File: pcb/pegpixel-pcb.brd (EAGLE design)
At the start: 23.1 x 17.2 mm, 14 parts

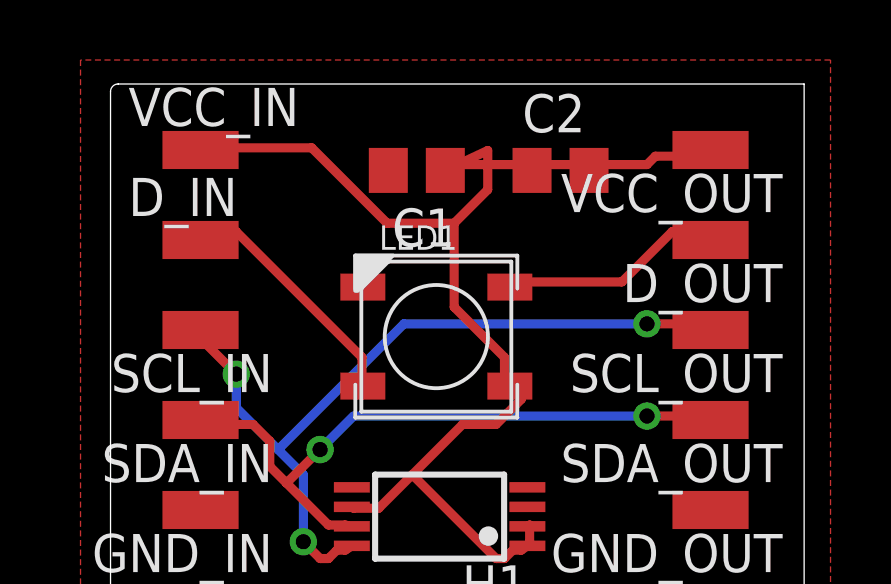
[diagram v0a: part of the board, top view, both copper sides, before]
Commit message: Add second capacitor to schema #2
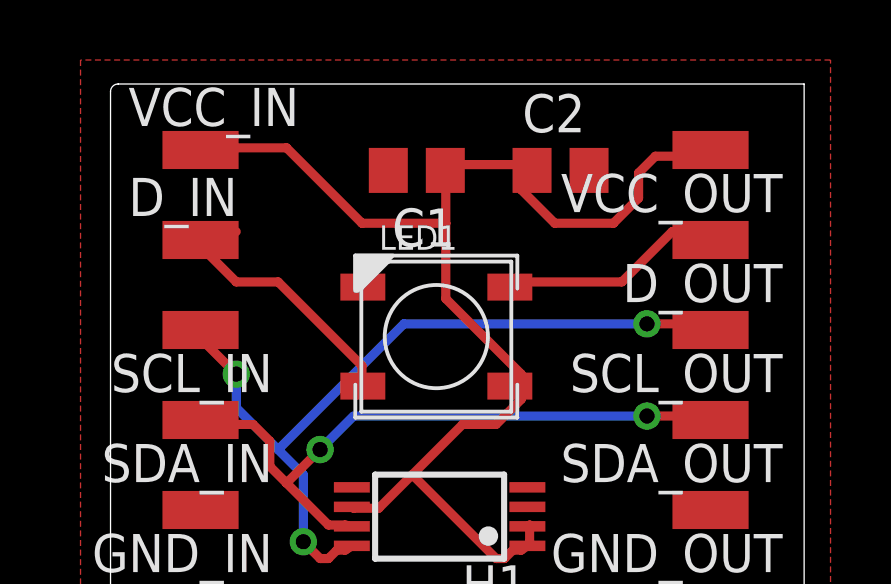
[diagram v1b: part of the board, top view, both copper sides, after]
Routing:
- net N$2: track 43.3 -> 44.7 mm
- net N$6: track 8.29 -> 9.62 mm
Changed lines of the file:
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@@
 <contactref element="VCC_IN" pad="1"/>
 <contactref element="VCC_OUT" pad="1"/>
+<contactref element="C2" pad="1"/>
+<wire x1="13.97" y1="21.5138" x2="13.6906" y2="21.5138" width="0.3048" layer="1"/>
+<wire x1="13.6906" y1="21.5138" x2="11.176" y2="21.5138" width="0.3048" layer="1"/>
+<wire x1="11.176" y1="21.5138" x2="11.16" y2="21.32" width="0.3048" layer="1"/>
+<wire x1="13.97" y1="21.5138" x2="14.05" y2="21.32" width="0.3048" layer="1"/>
 <wire x1="13.97" y1="9.4996" x2="13.97" y2="8.9408" width="0.3048" layer="1"/>
 <wire x1="13.97" y1="8.9408" x2="13.895" y2="8.805" width="0.3048" layer="1"/>
@@
 <wire x1="10.0584" y1="11.176" x2="12.8524" y2="8.382" width="0.3048" layer="1"/>
 <wire x1="13.6906" y1="8.6614" x2="13.895" y2="8.805" width="0.3048" layer="1"/>
-<wire x1="17.8816" y1="21.5138" x2="12.573" y2="21.5138" width="0.3048" layer="1"/>
-<wire x1="12.573" y1="21.5138" x2="11.2936" y2="21.5138" width="0.3048" layer="1"/>
-<wire x1="18.161" y1="21.7932" x2="17.8816" y2="21.5138" width="0.3048" layer="1"/>
-<wire x1="19.8374" y1="21.7932" x2="18.161" y2="21.7932" width="0.3048" layer="1"/>
-<wire x1="11.2936" y1="21.5138" x2="11.16" y2="21.32" width="0.3048" layer="1"/>
+<wire x1="11.176" y1="17.0434" x2="11.176" y2="19.558" width="0.3048" layer="1"/>
+<wire x1="11.176" y1="19.558" x2="11.176" y2="21.2344" width="0.3048" layer="1"/>
+<wire x1="13.6906" y1="14.5288" x2="11.176" y2="17.0434" width="0.3048" layer="1"/>
+<wire x1="13.6906" y1="13.97" x2="13.6906" y2="14.5288" width="0.3048" layer="1"/>
+<wire x1="11.176" y1="21.2344" x2="11.16" y2="21.32" width="0.3048" layer="1"/>
+<wire x1="13.6906" y1="13.97" x2="13.31" y2="14.13" width="0.3048" layer="1"/>
+<wire x1="5.8674" y1="22.0726" x2="3.0734" y2="22.0726" width="0.3048" layer="1"/>
+<wire x1="8.382" y1="19.558" x2="5.8674" y2="22.0726" width="0.3048" layer="1"/>
+<wire x1="11.176" y1="19.558" x2="8.382" y2="19.558" width="0.3048" layer="1"/>
+<wire x1="3.0734" y1="22.0726" x2="3" y2="22" width="0.3048" layer="1"/>
+<wire x1="18.161" y1="21.7932" x2="19.8374" y2="21.7932" width="0.3048" layer="1"/>
+<wire x1="17.6022" y1="21.2344" x2="18.161" y2="21.7932" width="0.3048" layer="1"/>
+<wire x1="17.6022" y1="20.3962" x2="17.6022" y2="21.2344" width="0.3048" layer="1"/>
+<wire x1="16.764" y1="19.558" x2="17.6022" y2="20.3962" width="0.3048" layer="1"/>
+<wire x1="14.8082" y1="19.558" x2="16.764" y2="19.558" width="0.3048" layer="1"/>
+<wire x1="13.6906" y1="20.6756" x2="14.8082" y2="19.558" width="0.3048" layer="1"/>
+<wire x1="13.6906" y1="21.5138" x2="13.6906" y2="20.6756" width="0.3048" layer="1"/>
 <wire x1="19.8374" y1="21.7932" x2="20" y2="22" width="0.3048" layer="1"/>
-<wire x1="6.7056" y1="22.0726" x2="3.0734" y2="22.0726" width="0.3048" layer="1"/>
-<wire x1="9.2202" y1="19.558" x2="6.7056" y2="22.0726" width="0.3048" layer="1"/>
-<wire x1="11.4554" y1="19.558" x2="9.2202" y2="19.558" width="0.3048" layer="1"/>
-<wire x1="12.573" y1="20.6756" x2="11.4554" y2="19.558" width="0.3048" layer="1"/>
-<wire x1="12.573" y1="21.98305" x2="12.573" y2="21.5138" width="0.3048" layer="1"/>
-<wire x1="12.573" y1="21.5138" x2="12.573" y2="20.6756" width="0.3048" layer="1"/>
-<wire x1="3.0734" y1="22.0726" x2="3" y2="22" width="0.3048" layer="1"/>
-<wire x1="12.573" y1="21.98305" x2="11.16" y2="21.32" width="0.3048" layer="1"/>
-<wire x1="13.1318" y1="15.0876" x2="13.1318" y2="14.2494" width="0.3048" layer="1"/>
-<wire x1="11.4554" y1="16.764" x2="13.1318" y2="15.0876" width="0.3048" layer="1"/>
-<wire x1="11.4554" y1="19.558" x2="11.4554" y2="16.764" width="0.3048" layer="1"/>
-<wire x1="13.1318" y1="14.2494" x2="13.31" y2="14.13" width="0.3048" layer="1"/>
-<contactref element="C2" pad="1"/>
-<wire x1="14.05" y1="21.32" x2="8.045" y2="10.105" width="0" layer="19" extent="1-1"/>
+<wire x1="13.6906" y1="21.5138" x2="14.05" y2="21.32" width="0.3048" layer="1"/>
 </signal>
 <signal name="N$4">
@@
 <contactref element="LED1" pad="4-DIN"/>
 <contactref element="D_IN" pad="1"/>
-<wire x1="8.382" y1="15.0876" x2="8.382" y2="14.2494" width="0.3048" layer="1"/>
-<wire x1="4.191" y1="19.2786" x2="8.382" y2="15.0876" width="0.3048" layer="1"/>
 <wire x1="3.0734" y1="19.2786" x2="4.191" y2="19.2786" width="0.3048" layer="1"/>
+<wire x1="3.0734" y1="19.2786" x2="3" y2="19" width="0.3048" layer="1"/>
+<wire x1="8.382" y1="14.8082" x2="8.382" y2="14.2494" width="0.3048" layer="1"/>
+<wire x1="5.588" y1="17.6022" x2="8.382" y2="14.8082" width="0.3048" layer="1"/>
+<wire x1="4.191" y1="17.6022" x2="5.588" y2="17.6022" width="0.3048" layer="1"/>
+<wire x1="2.794" y1="18.9992" x2="4.191" y2="17.6022" width="0.3048" layer="1"/>
 <wire x1="8.382" y1="14.2494" x2="8.41" y2="14.13" width="0.3048" layer="1"/>
-<wire x1="3.0734" y1="19.2786" x2="3" y2="19" width="0.3048" layer="1"/>
+<wire x1="2.794" y1="18.9992" x2="3" y2="19" width="0.3048" layer="1"/>
 </signal>
 <signal name="N$7">
@@
 </polygon>
 <contactref element="C2" pad="2"/>
-<wire x1="8.41" y1="17.43" x2="9.26" y2="21.32" width="0" layer="19" extent="1-1"/>
-<wire x1="13.895" y1="10.105" x2="8.41" y2="17.43" width="0" layer="19" extent="1-1"/>
-<wire x1="20" y1="10" x2="13.895" y2="10.105" width="0" layer="19" extent="1-1"/>
-<wire x1="3" y1="10" x2="8.41" y2="17.43" width="0" layer="19" extent="1-1"/>
-<wire x1="15.95" y1="21.32" x2="3" y2="10" width="0" layer="19" extent="1-1"/>
 </signal>
 </signals>

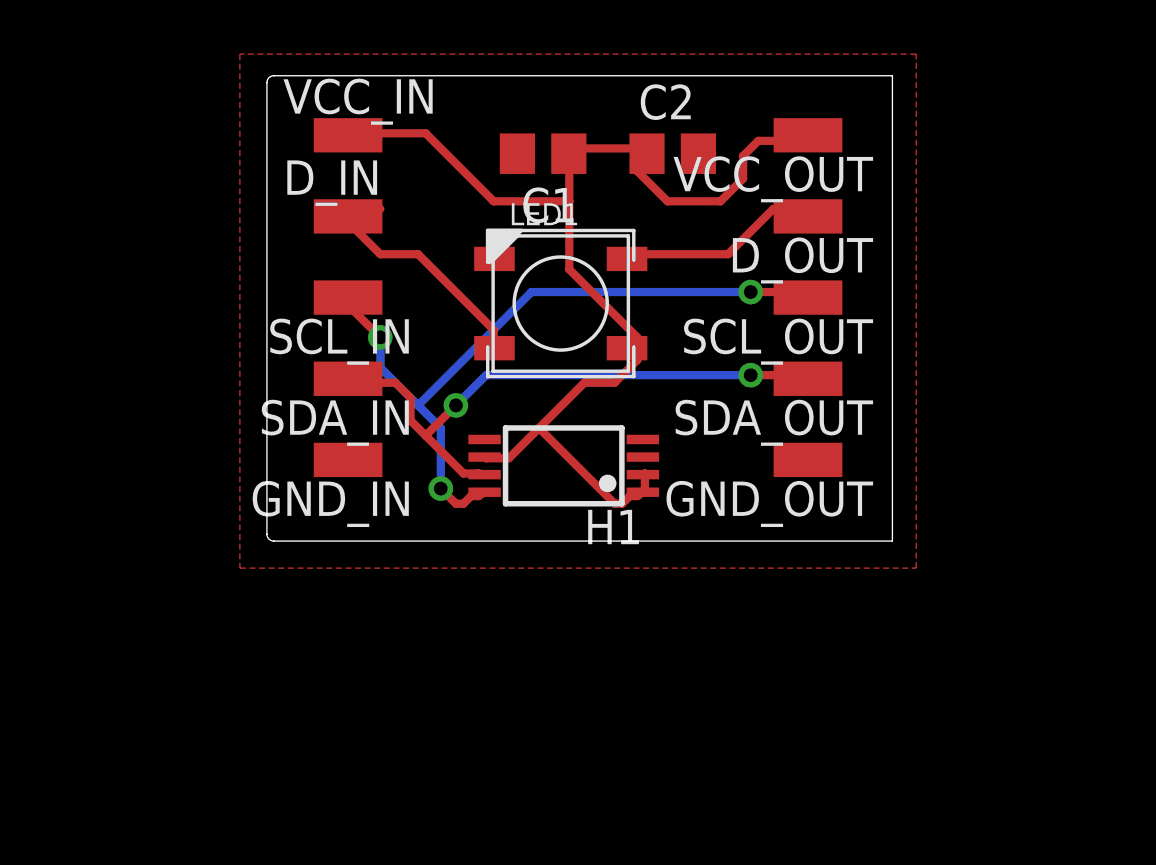
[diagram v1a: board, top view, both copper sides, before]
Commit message: pcb-design: delete design with solder-points
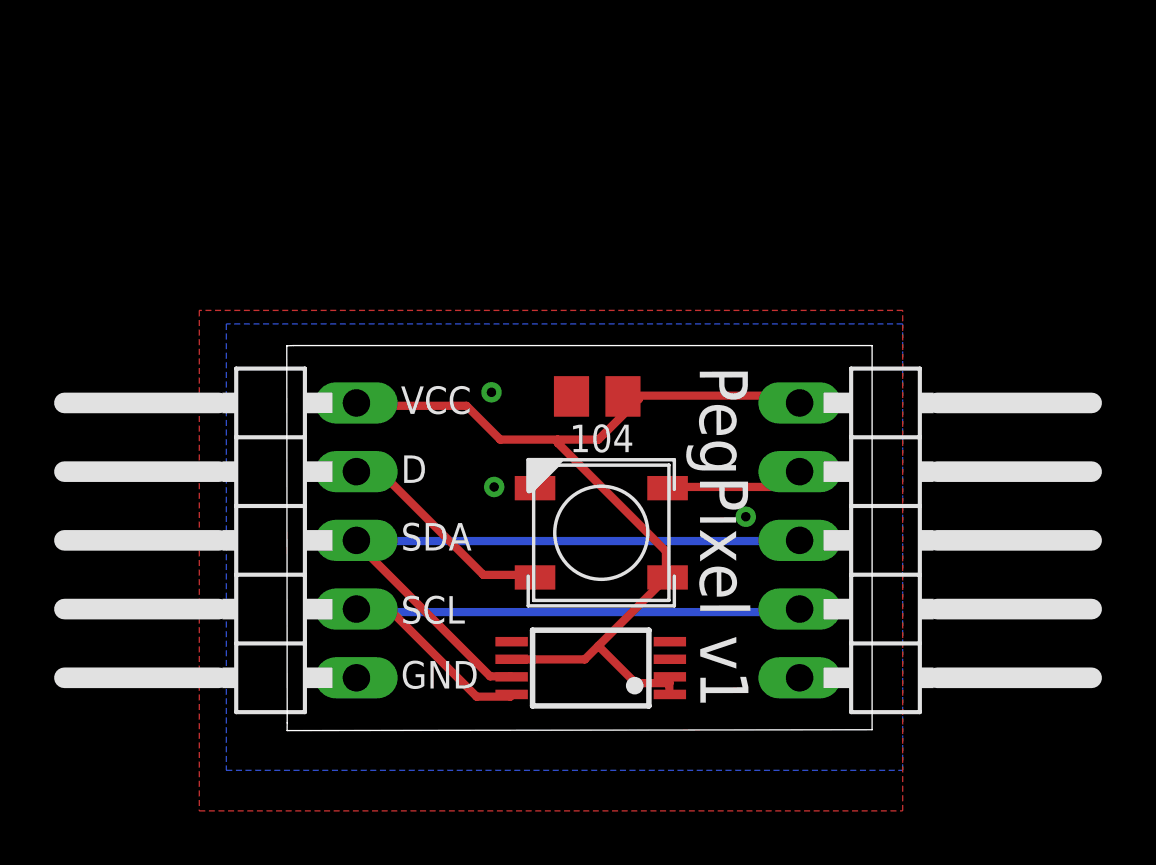
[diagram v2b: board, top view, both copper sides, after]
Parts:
- removed C1, C2: 104, rcl:C0805
- removed D_IN, D_OUT, GND_IN, GND_OUT, SCL_IN, SCL_OUT, SDA_IN, SDA_OUT, VCC_IN, VCC_OUT: WIREPADSMD1,27-254, wirepad:SMD1,27-2,54
- added 104: 104, rcl:C0805
- added JP1, JP2: (no value), pinhead:1X05/90
- moved LED1 8.61 mm to (12.4, 7.31)
- moved H1 7.54 mm to (12.0, 2.31)
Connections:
- removed net N$2: C1.1, C2.1, H1.1, H1.2, H1.6, LED1.1-VDD, VCC_IN.1, VCC_OUT.1
- removed net N$4: H1.8, SCL_IN.1, SCL_OUT.1
- removed net N$5: H1.7, SDA_IN.1, SDA_OUT.1
- removed net N$6: D_IN.1, LED1.4-DIN
- removed net N$7: D_OUT.1, LED1.2-DOUT
- new net DIN: JP1.4, LED1.4-DIN
- new net DOUT: JP2.2, LED1.2-DOUT
- new net SCL: H1.8, JP1.2, JP2.4
- new net SDA: H1.7, JP1.3, JP2.3
- new net VCC: 104.1, H1.1, H1.2, H1.6, JP1.5, JP2.1, LED1.1-VDD
- net GND: now also 104.2, JP1.1, JP2.5; no longer C1.2, C2.2, GND_IN.1, GND_OUT.1
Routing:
- net N$2: track 44.7 -> 0.00 mm
- net VCC: track 0.00 -> 36.5 mm
- net N$4: track 27.0 -> 0.00 mm, vias 3 -> 0
- net SDA: track 0.00 -> 24.3 mm
- net SCL: track 0.00 -> 23.6 mm
- net N$5: track 22.1 -> 0.00 mm, vias 2 -> 0
- net N$6: track 9.62 -> 0.00 mm
- net DIN: track 0.00 -> 8.25 mm
- net N$7: track 7.64 -> 0.00 mm
- net DOUT: track 0.00 -> 5.13 mm
- added copper zone on layer 16, net GND
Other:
- board size 23.1 x 17.2 mm -> 21.6 x 14.2 mm
- board text added: "D"
- board text added: "GND"
- board text added: "PegPıxel v1"
- board text added: "SCL"
- board text added: "SDA"
- board text added: "VCC"
